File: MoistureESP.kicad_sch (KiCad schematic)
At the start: 10 parts, among them J1 Conn_01x03_Pin, J2 Conn_MoisturePCB, J3 Conn_DS18B20, J5 Conn_01x04_Pin, J6 Conn_01x02_Pin, J7 Conn_01x06_Pin, SW1 147873-1

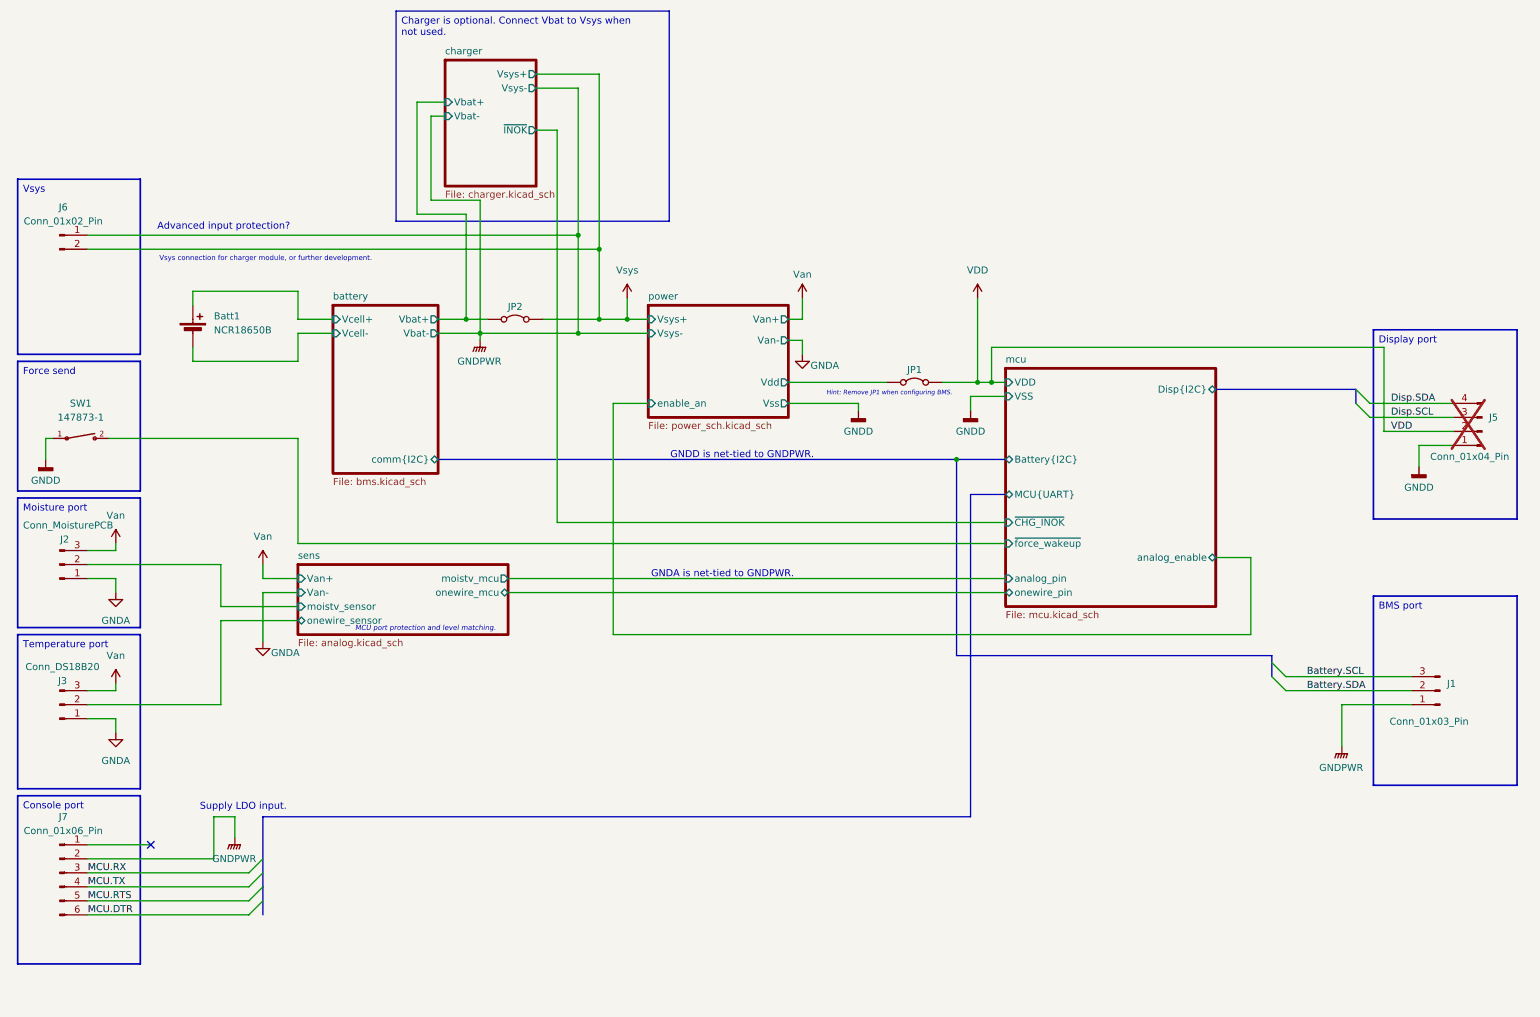
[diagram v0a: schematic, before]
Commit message: Add protected Vbat charger input.
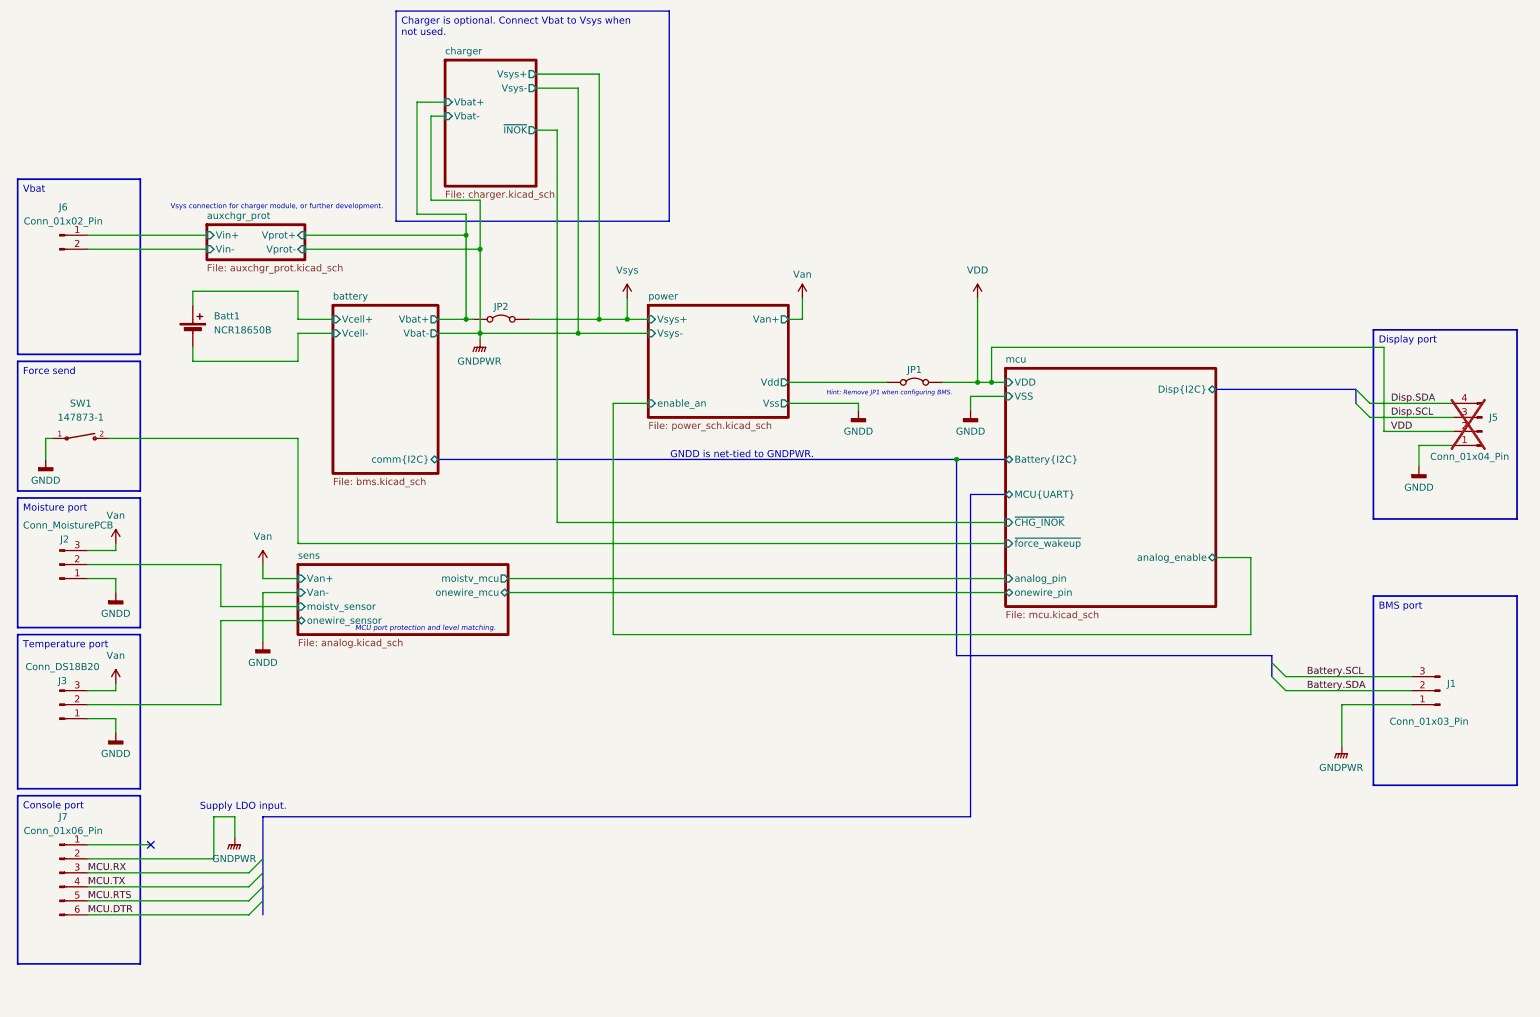
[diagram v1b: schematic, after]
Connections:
- net GNDA is gone; now on net GNDD: J2.1 (Pin_1), J3.1 (Pin_1)
- net GNDPWR: no longer J6.1 (Pin_1)
- net Vsys: no longer J6.2 (Pin_2)
- net battery/Vbat+ renamed auxchgr_prot/Vprot+
- new net auxchgr_prot/Vin+: J6.1 (Pin_1)
- new net auxchgr_prot/Vin-: J6.2 (Pin_2)
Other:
- added sheet auxchgr_prot (auxchgr_prot.kicad_sch)
- sheet power ports: added none; removed Van-
- note removed: "Advanced input protection?"
- note removed: "GNDA is net-tied to GNDPWR."
- moved on the sheet: JP2

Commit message: Add footprint to debug connector.
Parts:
- J7: footprint (none) -> Connector_PinHeader_2.54mm:PinHeader_1x06_P2.54mm_Vertical
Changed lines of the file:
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@@
 			)
 		)
-		(property "Footprint" ""
+		(property "Footprint" "Connector_PinHeader_2.54mm:PinHeader_1x06_P2.54mm_Vertical"
 			(at 20.32 170.18 0)
 			(hide yes)

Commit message: Start placement
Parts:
- J1: footprint Connector_PinHeader_2.54mm:PinHeader_1x03_P2.54mm_Horizontal -> Connector_PinHeader_2.54mm:PinHeader_1x03_P2.54mm_Vertical
- J6: footprint (none) -> Connector_PinHeader_2.54mm:PinHeader_1x02_P2.54mm_Vertical
- JP1, JP2: footprint Connector_PinHeader_2.54mm:PinHeader_1x02_P2.54mm_Horizontal -> Connector_PinHeader_2.54mm:PinHeader_1x02_P2.54mm_Vertical
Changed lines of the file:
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@@
 			)
 		)
-		(property "Footprint" ""
+		(property "Footprint" "Connector_PinHeader_2.54mm:PinHeader_1x02_P2.54mm_Vertical"
 			(at 20.32 54.61 0)
 			(hide yes)
@@
 			)
 		)
-		(property "Footprint" "Connector_PinHeader_2.54mm:PinHeader_1x03_P2.54mm_Horizontal"
+		(property "Footprint" "Connector_PinHeader_2.54mm:PinHeader_1x03_P2.54mm_Vertical"
 			(at 270.51 137.16 0)
 			(hide yes)
@@
 			)
 		)
-		(property "Footprint" "Connector_PinHeader_2.54mm:PinHeader_1x02_P2.54mm_Horizontal"
+		(property "Footprint" "Connector_PinHeader_2.54mm:PinHeader_1x02_P2.54mm_Vertical"
 			(at 100.33 69.85 0)
 			(hide yes)
@@
 			)
 		)
-		(property "Footprint" "Connector_PinHeader_2.54mm:PinHeader_1x02_P2.54mm_Horizontal"
+		(property "Footprint" "Connector_PinHeader_2.54mm:PinHeader_1x02_P2.54mm_Vertical"
 			(at 175.26 81.28 0)
 			(hide yes)

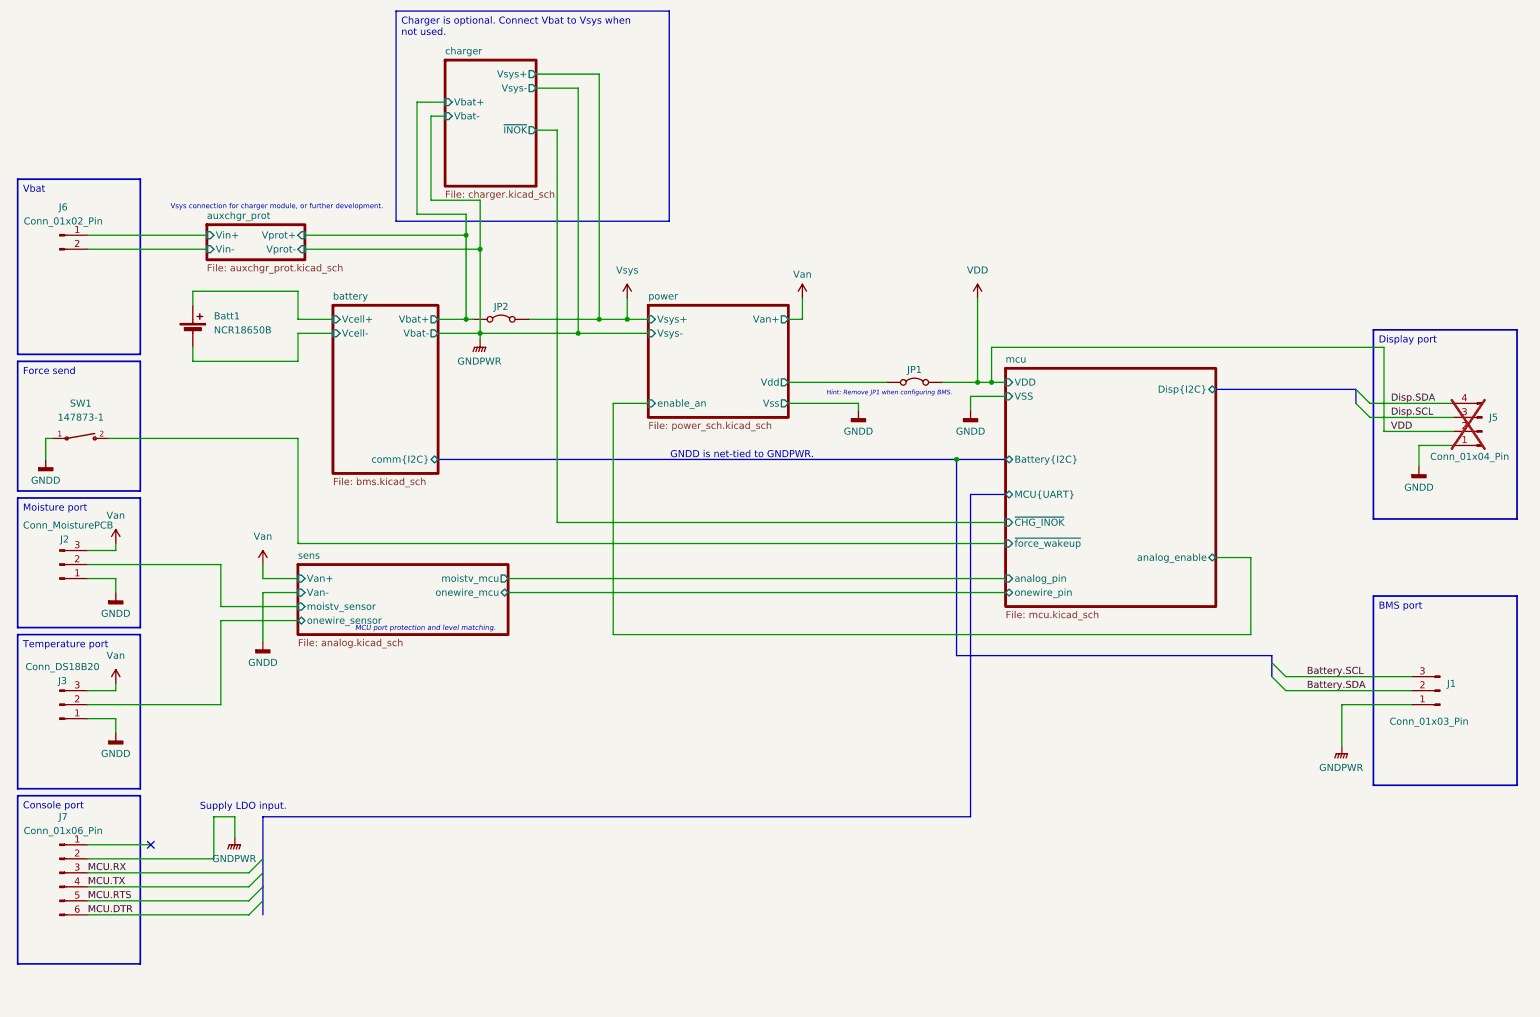
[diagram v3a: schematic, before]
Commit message: Add wiring, change footprint to avoid fatal errors at pads.
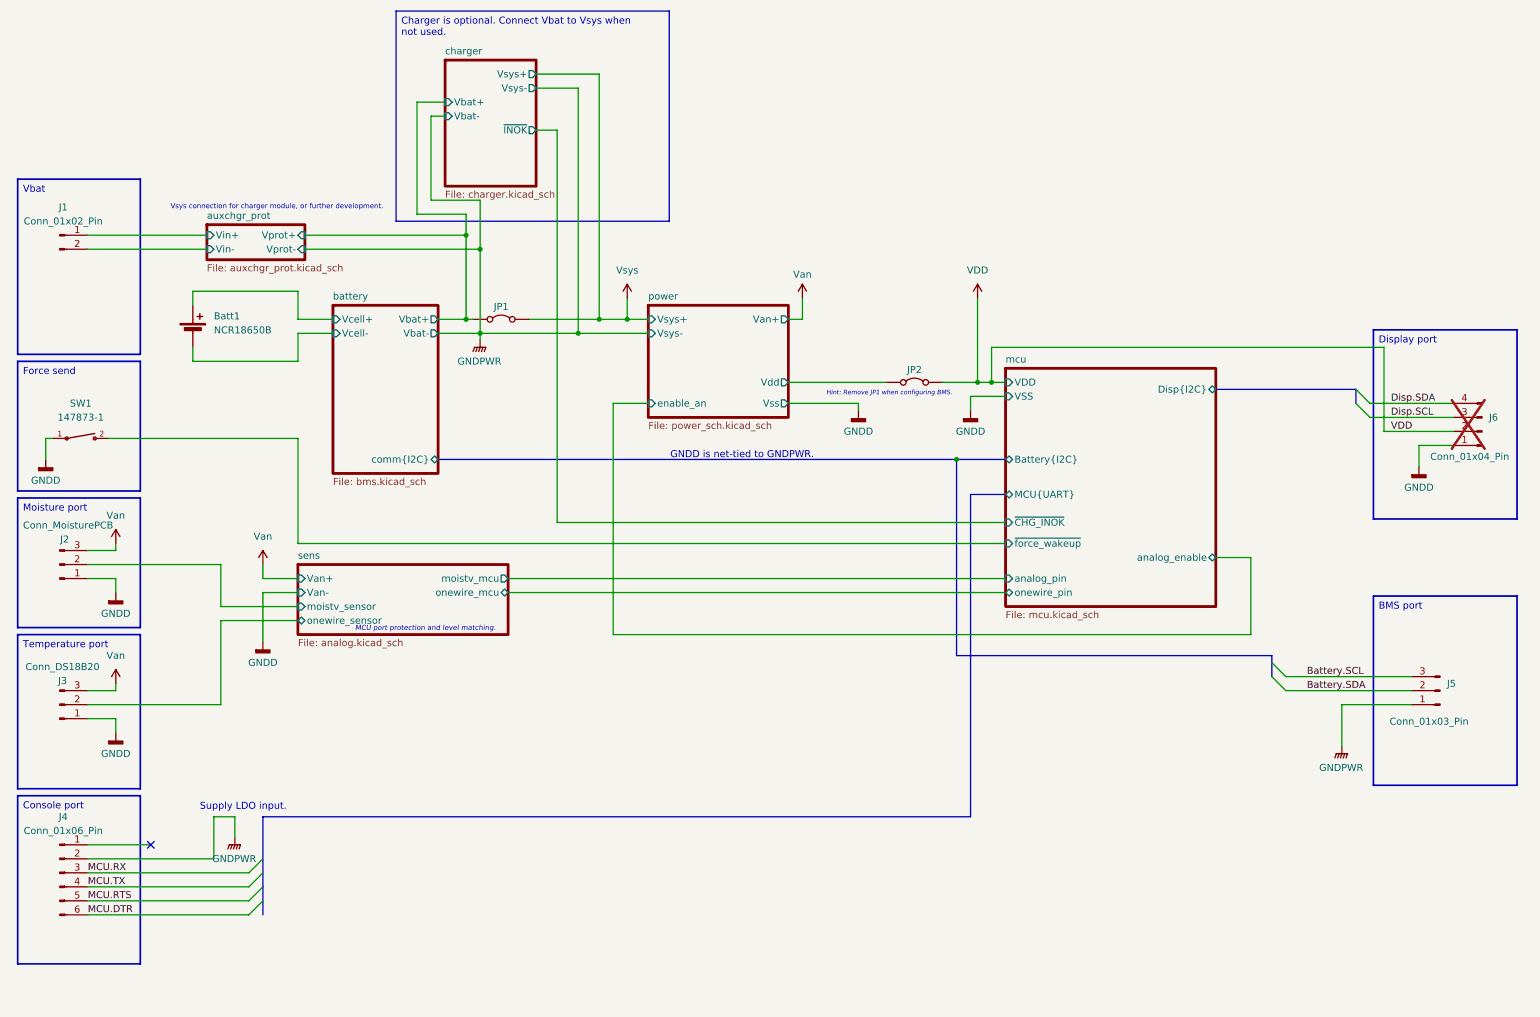
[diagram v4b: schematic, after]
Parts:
- renumbered J6 to J1, J7 to J4, J1 to J5, J5 to J6, JP2 to JP1, JP1 to JP2
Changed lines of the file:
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@@
 		(in_pos_files yes)
 		(dnp yes)
-		(property "Reference" "J5"
+		(property "Reference" "J6"
 			(at 279.4 87.6299 0)
 			(show_name no)
@@
 			(project "MoistureESP"
 				(path "/f2b9f638-139e-46ec-aa60-77c4af989196"
-					(reference "J5")
+					(reference "J6")
 					(unit 1)
 				)
@@
 		(dnp no)
 		(fields_autoplaced yes)
-		(property "Reference" "J6"
+		(property "Reference" "J1"
 			(at 20.955 49.53 0)
 			(show_name no)
@@
 			(project "MoistureESP"
 				(path "/f2b9f638-139e-46ec-aa60-77c4af989196"
-					(reference "J6")
+					(reference "J1")
 					(unit 1)
 				)
@@
 		(in_pos_files yes)
 		(dnp no)
-		(property "Reference" "#PWR034"
+		(property "Reference" "#PWR011"
 			(at 154.94 69.85 0)
 			(hide yes)
@@
 			(project "MoistureESP"
 				(path "/f2b9f638-139e-46ec-aa60-77c4af989196"
-					(reference "#PWR034")
+					(reference "#PWR011")
 					(unit 1)
 				)
@@
 		(in_pos_files yes)
 		(dnp no)
-		(property "Reference" "J1"
+		(property "Reference" "J5"
 			(at 271.78 135.8899 0)
 			(show_name no)
@@
 			(project "MoistureESP"
 				(path "/f2b9f638-139e-46ec-aa60-77c4af989196"
-					(reference "J1")
+					(reference "J5")
 					(unit 1)
 				)
@@
 		(dnp no)
 		(fields_autoplaced yes)
-		(property "Reference" "#PWR012"
+		(property "Reference" "#PWR015"
 			(at 252.73 152.4 0)
 			(hide yes)
@@
 			(project "MoistureESP"
 				(path "/f2b9f638-139e-46ec-aa60-77c4af989196"
-					(reference "#PWR012")
+					(reference "#PWR015")
 					(unit 1)
 				)
@@
 		(dnp no)
 		(fields_autoplaced yes)
-		(property "Reference" "#PWR014"
+		(property "Reference" "#PWR013"
 			(at 185.42 92.71 0)
 			(hide yes)
@@
 			(project "MoistureESP"
 				(path "/f2b9f638-139e-46ec-aa60-77c4af989196"
-					(reference "#PWR014")
+					(reference "#PWR013")
 					(unit 1)
 				)
@@
 		(dnp no)
 		(fields_autoplaced yes)
-		(property "Reference" "#PWR025"
+		(property "Reference" "#PWR03"
 			(at 30.48 125.73 0)
 			(hide yes)
@@
 			(project "MoistureESP"
 				(path "/f2b9f638-139e-46ec-aa60-77c4af989196"
-					(reference "#PWR025")
+					(reference "#PWR03")
 					(unit 1)
 				)
@@
 		(dnp no)
 		(fields_autoplaced yes)
-		(property "Reference" "#PWR070"
+		(property "Reference" "#PWR06"
 			(at 52.07 168.91 0)
 			(hide yes)
@@
 			(project "MoistureESP"
 				(path "/f2b9f638-139e-46ec-aa60-77c4af989196"
-					(reference "#PWR070")
+					(reference "#PWR06")
 					(unit 1)
 				)
@@
 		(dnp no)
 		(fields_autoplaced yes)
-		(property "Reference" "#PWR047"
+		(property "Reference" "#PWR016"
 			(at 266.7 102.87 0)
 			(hide yes)
@@
 			(project "MoistureESP"
 				(path "/f2b9f638-139e-46ec-aa60-77c4af989196"
-					(reference "#PWR047")
+					(reference "#PWR016")
 					(unit 1)
 				)
@@
 		(dnp no)
 		(fields_autoplaced yes)
-		(property "Reference" "#PWR035"
+		(property "Reference" "#PWR07"
 			(at 57.15 118.11 0)
 			(hide yes)
@@
 			(project "MoistureESP"
 				(path "/f2b9f638-139e-46ec-aa60-77c4af989196"
-					(reference "#PWR035")
+					(reference "#PWR07")
 					(unit 1)
 				)
@@
 		(dnp no)
 		(fields_autoplaced yes)
-		(property "Reference" "#PWR016"
+		(property "Reference" "#PWR012"
 			(at 165.1 92.71 0)
 			(hide yes)
@@
 			(project "MoistureESP"
 				(path "/f2b9f638-139e-46ec-aa60-77c4af989196"
-					(reference "#PWR016")
+					(reference "#PWR012")
 					(unit 1)
 				)
@@
 		(in_pos_files yes)
 		(dnp no)
-		(property "Reference" "JP2"
+		(property "Reference" "JP1"
 			(at 100.33 67.564 0)
 			(show_name no)
@@
 			(project "MoistureESP"
 				(path "/f2b9f638-139e-46ec-aa60-77c4af989196"
-					(reference "JP2")
+					(reference "JP1")
 					(unit 1)
 				)
@@
 		(dnp no)
 		(fields_autoplaced yes)
-		(property "Reference" "#PWR069"
+		(property "Reference" "#PWR010"
 			(at 123.19 69.85 0)
 			(hide yes)
@@
 			(project "MoistureESP"
 				(path "/f2b9f638-139e-46ec-aa60-77c4af989196"
-					(reference "#PWR069")
+					(reference "#PWR010")
 					(unit 1)
 				)
@@
 		(in_pos_files yes)
 		(dnp no)
-		(property "Reference" "JP1"
+		(property "Reference" "JP2"
 			(at 175.26 78.994 0)
 			(show_name no)
@@
 			(project "MoistureESP"
 				(path "/f2b9f638-139e-46ec-aa60-77c4af989196"
-					(reference "JP1")
+					(reference "JP2")
 					(unit 1)
 				)
@@
 		(dnp no)
 		(fields_autoplaced yes)
-		(property "Reference" "#PWR026"
+		(property "Reference" "#PWR08"
 			(at 57.15 134.62 0)
 			(hide yes)
@@
 			(project "MoistureESP"
 				(path "/f2b9f638-139e-46ec-aa60-77c4af989196"
-					(reference "#PWR026")
+					(reference "#PWR08")
 					(unit 1)
 				)
@@
 		(dnp no)
 		(fields_autoplaced yes)
-		(property "Reference" "#PWR045"
+		(property "Reference" "#PWR01"
 			(at 17.78 101.6 0)
 			(hide yes)
@@
 			(project "MoistureESP"
 				(path "/f2b9f638-139e-46ec-aa60-77c4af989196"
-					(reference "#PWR045")
+					(reference "#PWR01")
 					(unit 1)
 				)
@@
 		(dnp no)
 		(fields_autoplaced yes)
-		(property "Reference" "#PWR038"
+		(property "Reference" "#PWR02"
 			(at 30.48 114.3 0)
 			(hide yes)
@@
 			(project "MoistureESP"
 				(path "/f2b9f638-139e-46ec-aa60-77c4af989196"
-					(reference "#PWR038")
+					(reference "#PWR02")
 					(unit 1)
 				)
@@
 		(dnp no)
 		(fields_autoplaced yes)
-		(property "Reference" "#PWR067"
+		(property "Reference" "#PWR014"
 			(at 186.69 69.85 0)
 			(hide yes)
@@
 			(project "MoistureESP"
 				(path "/f2b9f638-139e-46ec-aa60-77c4af989196"
-					(reference "#PWR067")
+					(reference "#PWR014")
 					(unit 1)
 				)
@@
 		(dnp no)
 		(fields_autoplaced yes)
-		(property "Reference" "#PWR024"
+		(property "Reference" "#PWR05"
 			(at 30.48 151.13 0)
 			(hide yes)
@@
 			(project "MoistureESP"
 				(path "/f2b9f638-139e-46ec-aa60-77c4af989196"
-					(reference "#PWR024")
+					(reference "#PWR05")
 					(unit 1)
 				)
@@
 		(dnp no)
 		(fields_autoplaced yes)
-		(property "Reference" "J7"
+		(property "Reference" "J4"
 			(at 20.955 160.02 0)
 			(show_name no)
@@
 			(project "MoistureESP"
 				(path "/f2b9f638-139e-46ec-aa60-77c4af989196"
-					(reference "J7")
+					(reference "J4")
 					(unit 1)
 				)
@@
 		(dnp no)
 		(fields_autoplaced yes)
-		(property "Reference" "#PWR060"
+		(property "Reference" "#PWR09"
 			(at 96.52 78.74 0)
 			(hide yes)
@@
 			(project "MoistureESP"
 				(path "/f2b9f638-139e-46ec-aa60-77c4af989196"
-					(reference "#PWR060")
+					(reference "#PWR09")
 					(unit 1)
 				)
@@
 		(dnp no)
 		(fields_autoplaced yes)
-		(property "Reference" "#PWR039"
+		(property "Reference" "#PWR04"
 			(at 30.48 139.7 0)
 			(hide yes)
@@
 			(project "MoistureESP"
 				(path "/f2b9f638-139e-46ec-aa60-77c4af989196"
-					(reference "#PWR039")
-					(unit 1)
-				)
+					(reference "#PWR04")
+					(unit 1)
+				)
